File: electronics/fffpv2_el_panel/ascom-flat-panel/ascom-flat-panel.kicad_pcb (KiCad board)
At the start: 2 copper layers, 55 x 46.6 mm, 20 parts, among them J1 Servo, J2 Conn_01x02, Q1 IRLZ34N, Q2 IRLZ34N, U1 XIAO-SAMD21-DIP, U2 TLC272

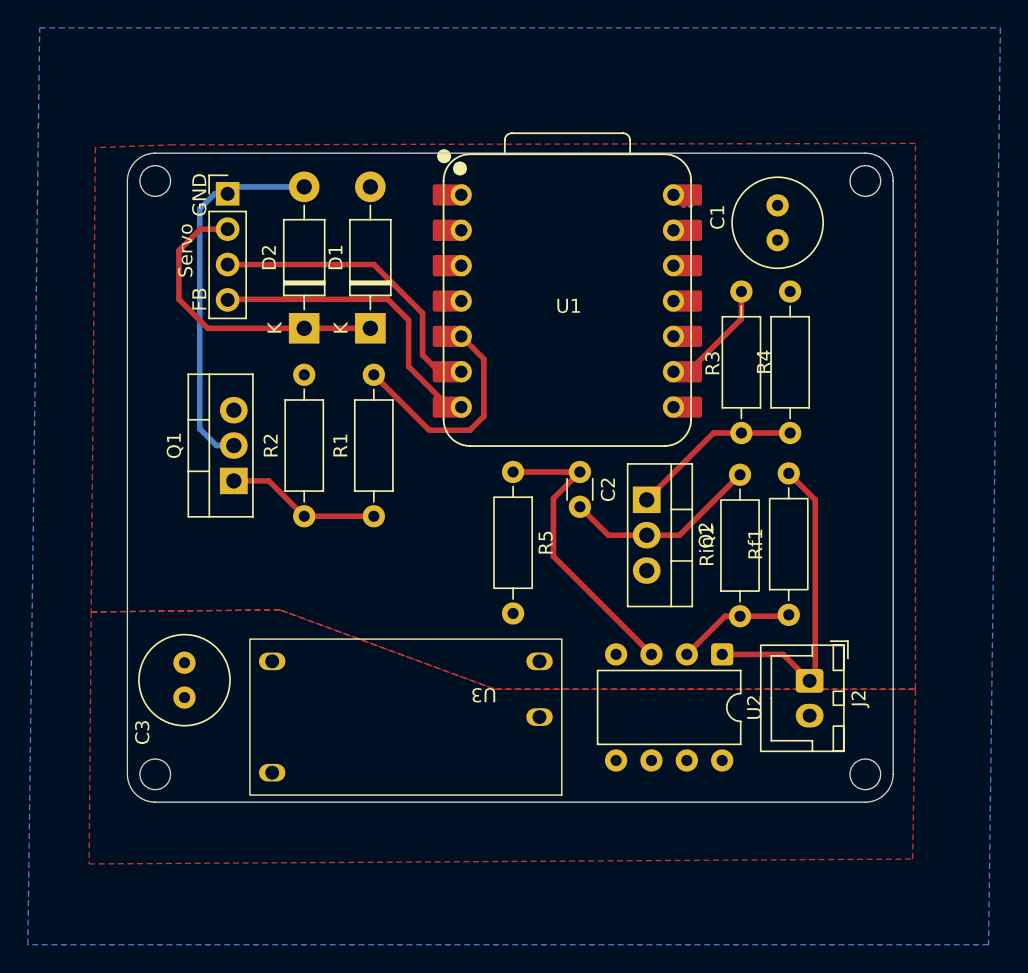
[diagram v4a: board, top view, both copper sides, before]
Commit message: Correction de l'empreinte du convertisseur DC DC + ajustements inhérents sur PCB + corrections cosmétiques sur PCB
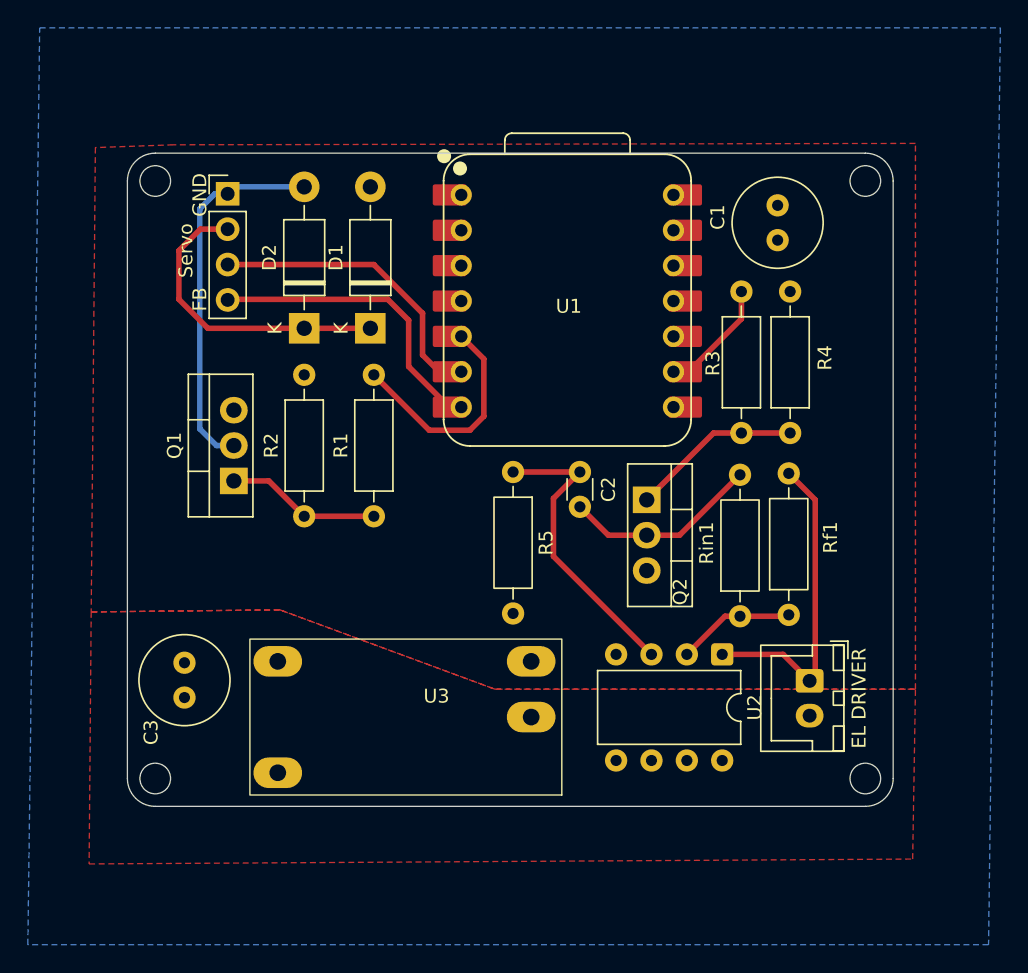
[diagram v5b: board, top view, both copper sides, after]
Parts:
- EL DRIVER: renamed from J2
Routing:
- net +5V: track 2.60 -> 0.48 mm
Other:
- board size 55 x 46.6 mm -> 55 x 46.9 mm

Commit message: Removed most warnings form ERC (schema) and DRC (pcb)
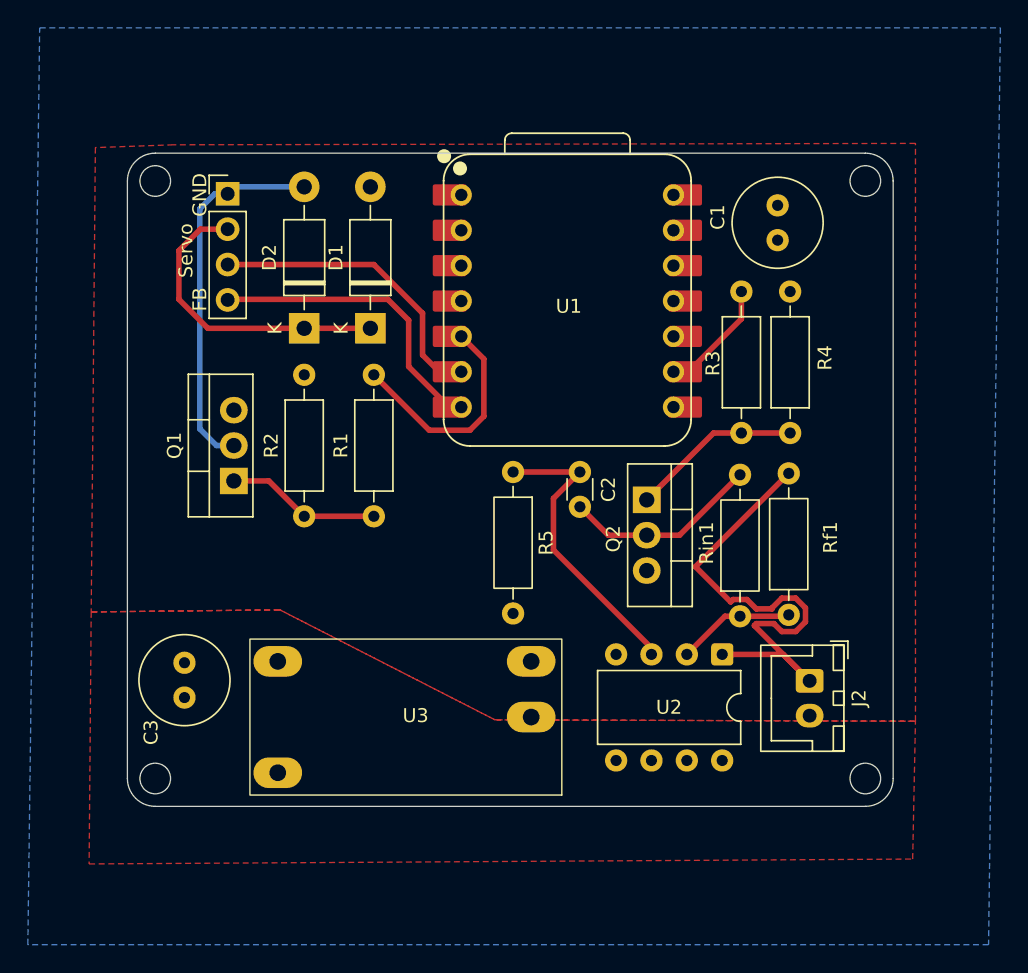
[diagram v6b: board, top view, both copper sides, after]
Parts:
- J2: renamed from EL DRIVER
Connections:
- U2 pad 5: (no net) -> unconnected-(U2B-+-Pad5)
- U2 pad 6: (no net) -> unconnected-(U2B---Pad6)
- U2 pad 7: (no net) -> unconnected-(U2-Pad7)
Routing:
- net EL_DRIVER+: track 22.9 -> 37.4 mm
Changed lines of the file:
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@@
 	(net 22 "EL_DRIVER+")
 	(net 23 "Net-(U2A--)")
+	(net 24 "unconnected-(U1-PA02_A0_D0-Pad1)_1")
+	(net 25 "unconnected-(U1-PB09_A7_D7_RX-Pad8)_1")
+	(net 26 "unconnected-(U1-PA4_A1_D1-Pad2)_1")
+	(net 27 "unconnected-(U1-PA6_A10_D10_MOSI-Pad11)_1")
+	(net 28 "unconnected-(U1-3V3-Pad12)_1")
+	(net 29 "unconnected-(U1-PA5_A9_D9_MISO-Pad10)_1")
+	(net 30 "unconnected-(U1-PA11_A3_D3-Pad4)_1")
+	(net 31 "unconnected-(U1-PA10_A2_D2-Pad3)_1")
+	(net 32 "unconnected-(U2B---Pad6)")
+	(net 33 "unconnected-(U2-Pad7)")
+	(net 34 "unconnected-(U2B-+-Pad5)")
 	(footprint "Connector_JST:JST_XH_B2B-XH-A_1x02_P2.50mm_Vertical"
 		(layer "F.Cu")
@@
 		(descr "JST XH series connector, B2B-XH-A (http://www.jst-mfg.com/product/pdf/eng/eXH.pdf), generated with kicad-footprint-generator")
 		(tags "connector JST XH vertical")
-		(property "Reference" "EL DRIVER"
+		(property "Reference" "J2"
 			(at 1.25 -3.55 90)
 			(layer "F.SilkS")
@@
 			(layers "F.Cu" "F.Mask")
 			(roundrect_rratio 0.1)
-			(net 15 "unconnected-(U1-PA02_A0_D0-Pad1)")
+			(net 24 "unconnected-(U1-PA02_A0_D0-Pad1)_1")
 			(pinfunction "PA02_A0_D0")
-			(pintype "passive")
+			(pintype "passive+no_connect")
 			(thermal_bridge_angle 45)
 		)
@@
 			(net 15 "unconnected-(U1-PA02_A0_D0-Pad1)")
 			(pinfunction "PA02_A0_D0")
-			(pintype "passive")
+			(pintype "passive+no_connect")
 		)
 		(pad "2" smd roundrect
@@
 			(layers "F.Cu" "F.Mask")
 			(roundrect_rratio 0.1)
-			(net 16 "unconnected-(U1-PA4_A1_D1-Pad2)")
+			(net 26 "unconnected-(U1-PA4_A1_D1-Pad2)_1")
 			(pinfunction "PA4_A1_D1")
-			(pintype "passive")
+			(pintype "passive+no_connect")
 			(thermal_bridge_angle 45)
 		)
@@
 			(net 16 "unconnected-(U1-PA4_A1_D1-Pad2)")
 			(pinfunction "PA4_A1_D1")
-			(pintype "passive")
+			(pintype "passive+no_connect")
 		)
 		(pad "3" smd roundrect
@@
 			(net 14 "unconnected-(U1-PA10_A2_D2-Pad3)")
 			(pinfunction "PA10_A2_D2")
-			(pintype "passive")
+			(pintype "passive+no_connect")
 			(thermal_bridge_angle 45)
 		)
@@
 			(layers "*.Cu" "*.Mask")
 			(remove_unused_layers no)
-			(net 14 "unconnected-(U1-PA10_A2_D2-Pad3)")
+			(net 31 "unconnected-(U1-PA10_A2_D2-Pad3)_1")
 			(pinfunction "PA10_A2_D2")
-			(pintype "passive")
+			(pintype "passive+no_connect")
 		)
 		(pad "4" smd roundrect
@@
 			(net 12 "unconnected-(U1-PA11_A3_D3-Pad4)")
 			(pinfunction "PA11_A3_D3")
-			(pintype "passive")
+			(pintype "passive+no_connect")
 			(thermal_bridge_angle 45)
 		)
@@
 			(layers "*.Cu" "*.Mask")
 			(remove_unused_layers no)
-			(net 12 "unconnected-(U1-PA11_A3_D3-Pad4)")
+			(net 30 "unconnected-(U1-PA11_A3_D3-Pad4)_1")
 			(pinfunction "PA11_A3_D3")
-			(pintype "passive")
+			(pintype "passive+no_connect")
 		)
 		(pad "5" smd roundrect
@@
 			(net 17 "unconnected-(U1-PB09_A7_D7_RX-Pad8)")
 			(pinfunction "PB09_A7_D7_RX")
-			(pintype "passive")
+			(pintype "passive+no_connect")
 		)
 		(pad "8" smd roundrect
@@
 			(layers "F.Cu" "F.Mask")
 			(roundrect_rratio 0.1)
-			(net 17 "unconnected-(U1-PB09_A7_D7_RX-Pad8)")
+			(net 25 "unconnected-(U1-PB09_A7_D7_RX-Pad8)_1")
 			(pinfunction "PB09_A7_D7_RX")
-			(pintype "passive")
+			(pintype "passive+no_connect")
 			(thermal_bridge_angle 45)
 		)
@@
 			(net 13 "unconnected-(U1-PA5_A9_D9_MISO-Pad10)")
 			(pinfunction "PA5_A9_D9_MISO")
-			(pintype "passive")
+			(pintype "passive+no_connect")
 		)
 		(pad "10" smd roundrect
@@
 			(layers "F.Cu" "F.Mask")
 			(roundrect_rratio 0.1)
-			(net 13 "unconnected-(U1-PA5_A9_D9_MISO-Pad10)")
+			(net 29 "unconnected-(U1-PA5_A9_D9_MISO-Pad10)_1")
 			(pinfunction "PA5_A9_D9_MISO")
-			(pintype "passive")
+			(pintype "passive+no_connect")
 			(thermal_bridge_angle 45)
 		)
@@
 			(layers "*.Cu" "*.Mask")
 			(remove_unused_layers no)
-			(net 18 "unconnected-(U1-PA6_A10_D10_MOSI-Pad11)")
+			(net 27 "unconnected-(U1-PA6_A10_D10_MOSI-Pad11)_1")
 			(pinfunction "PA6_A10_D10_MOSI")
-			(pintype "passive")
+			(pintype "passive+no_connect")
 		)
 		(pad "11" smd roundrect
@@
 			(net 18 "unconnected-(U1-PA6_A10_D10_MOSI-Pad11)")
 			(pinfunction "PA6_A10_D10_MOSI")
-			(pintype "passive")
+			(pintype "passive+no_connect")
 			(thermal_bridge_angle 45)
 		)
@@
 			(layers "*.Cu" "*.Mask")
 			(remove_unused_layers no)
-			(net 7 "unconnected-(U1-3V3-Pad12)")
+			(net 28 "unconnected-(U1-3V3-Pad12)_1")
 			(pinfunction "3V3")
-			(pintype "passive")
+			(pintype "passive+no_connect")
 		)
 		(pad "12" smd roundrect
@@
 			(net 7 "unconnected-(U1-3V3-Pad12)")
 			(pinfunction "3V3")
-			(pintype "passive")
+			(pintype "passive+no_connect")
 			(thermal_bridge_angle 45)
 		)
@@
 		(tags "THT DIP DIL PDIP 2.54mm 7.62mm 300mil")
 		(property "Reference" "U2"
-			(at 3.81 -2.33 90)
+			(at 3.8 3.82 0)
 			(layer "F.SilkS")
 			(effects
@@
 			(layers "*.Cu" "*.Mask")
 			(remove_unused_layers no)
+			(net 34 "unconnected-(U2B-+-Pad5)")
+			(pinfunction "+")
+			(pintype "input+no_connect")
 		)
 		(pad "6" thru_hole circle
@@
 			(layers "*.Cu" "*.Mask")
 			(remove_unused_layers no)
+			(net 32 "unconnected-(U2B---Pad6)")
+			(pinfunction "-")
+			(pintype "input+no_connect")
 		)
 		(pad "7" thru_hole circle
@@
 			(layers "*.Cu" "*.Mask")
 			(remove_unused_layers no)
+			(net 33 "unconnected-(U2-Pad7)")
+			(pintype "output+no_connect")
 		)
 		(pad "8" thru_hole circle
@@
 		(tags "TO-220-3 Vertical RM 2.54mm")
 		(property "Reference" "Q2"
-			(at 6.6 -2.4 90)
+			(at 2.8 2.4 90)
 			(layer "F.SilkS")
 			(effects
@@
 		(at 116.3 110.6 180)
 		(property "Reference" "U3"
-			(at -2.2 1.6 0)
+			(at -0.7 0.2 0)
 			(unlocked yes)
 			(layer "F.SilkS")
@@
 	)
 	(segment
-		(start 126.9 94.8)
-		(end 126.9 98.96)
+		(start 128.8 92.9)
+		(end 126.9 94.8)
 		(width 0.4)
 		(layer "F.Cu")
@@
 	)
 	(segment
-		(start 126.9 98.96)
-		(end 133.94 106)
+		(start 126.9 98.5)
+		(end 133.94 105.54)
 		(width 0.4)
 		(layer "F.Cu")
@@
 	)
 	(segment
-		(start 128.8 92.9)
-		(end 126.9 94.8)
+		(start 124 92.9)
+		(end 128.8 92.9)
 		(width 0.4)
 		(layer "F.Cu")
@@
 	)
 	(segment
-		(start 124 92.9)
-		(end 128.8 92.9)
+		(start 126.9 94.8)
+		(end 126.9 98.5)
+		(width 0.4)
+		(layer "F.Cu")
+		(net 19)
+	)
+	(segment
+		(start 133.94 105.54)
+		(end 133.94 106)
 		(width 0.4)
 		(layer "F.Cu")
@@
 	(segment
 		(start 145.3 107.9)
-		(end 145.7 107.5)
+		(end 141.329235 103.929235)
+		(width 0.4)
+		(layer "F.Cu")
+		(net 22)
+	)
+	(segment
+		(start 145.001 102.662529)
+		(end 144.297471 101.959)
+		(width 0.4)
+		(layer "F.Cu")
+		(net 22)
+	)
+	(segment
+		(start 145.001 103.657471)
+		(end 145.001 102.662529)
+		(width 0.4)
+		(layer "F.Cu")
+		(net 22)
+	)
+	(segment
+		(start 140.797471 102.059)
+		(end 139.802529 102.059)
+		(width 0.4)
+		(layer "F.Cu")
+		(net 22)
+	)
+	(segment
+		(start 143.302529 101.959)
+		(end 142.599 102.662529)
+		(width 0.4)
+		(layer "F.Cu")
+		(net 22)
+	)
+	(segment
+		(start 144.297471 101.959)
+		(end 143.302529 101.959)
+		(width 0.4)
+		(layer "F.Cu")
+		(net 22)
+	)
+	(segment
+		(start 142.599 102.732)
+		(end 141.470471 102.732)
+		(width 0.4)
+		(layer "F.Cu")
+		(net 22)
+	)
+	(segment
+		(start 144.297471 104.361)
+		(end 145.001 103.657471)
+		(width 0.4)
+		(layer "F.Cu")
+		(net 22)
+	)
+	(segment
+		(start 141.470471 102.732)
+		(end 140.797471 102.059)
+		(width 0.4)
+		(layer "F.Cu")
+		(net 22)
+	)
+	(segment
+		(start 137.1 99.7)
+		(end 143.8 93)
 		(width 0.4)
 		(layer "F.Cu")
@@
 	)
 	(segment
+		(start 142.599 102.662529)
+		(end 142.599 102.732)
+		(width 0.4)
+		(layer "F.Cu")
+		(net 22)
+	)
+	(segment
+		(start 142.729529 103.788)
+		(end 143.302529 104.361)
+		(width 0.4)
+		(layer "F.Cu")
+		(net 22)
+	)
+	(segment
+		(start 141.470471 103.788)
+		(end 142.729529 103.788)
+		(width 0.4)
+		(layer "F.Cu")
+		(net 22)
+	)
+	(segment
 		(start 143.4 106)
 		(end 145.3 107.9)
@@
 	)
 	(segment
-		(start 145.7 94.9)
-		(end 143.8 93)
+		(start 143.302529 104.361)
+		(end 144.297471 104.361)
+		(width 0.4)
+		(layer "F.Cu")
+		(net 22)
+	)
+	(segment
+		(start 139.630764 102.230764)
+		(end 137.1 99.7)
+		(width 0.4)
+		(layer "F.Cu")
+		(net 22)
+	)
+	(segment
+		(start 141.329235 103.929235)
+		(end 141.470471 103.788)
 		(width 0.4)
 		(layer "F.Cu")
@@
 	)
 	(segment
-		(start 145.7 107.5)
-		(end 145.7 94.9)
+		(start 139.802529 102.059)
+		(end 139.630764 102.230764)
 		(width 0.4)
 		(layer "F.Cu")
@@
 		(polygon
 			(pts
-				(xy 93.7 102.95) (xy 93.55 121.05) (xy 152.7 120.7) (xy 152.9 108.5) (xy 122.7 108.5) (xy 107.25 102.8)
+				(xy 93.7 102.95) (xy 93.55 121.05) (xy 152.7 120.7) (xy 152.9 110.8) (xy 122.7 110.7) (xy 107.25 102.8)
 			)
 		)
@@
 		(polygon
 			(pts
-				(xy 94 69.6) (xy 93.7 102.95) (xy 107.25 102.8) (xy 122.7 108.5) (xy 152.9 108.5) (xy 152.9 69.3)
+				(xy 94 69.6) (xy 93.7 102.95) (xy 107.25 102.8) (xy 122.7 110.7) (xy 152.9 110.8) (xy 152.9 69.3)
 				(xy 99.6 69.4)
 			)

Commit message: Feedback from first breadboard prototype
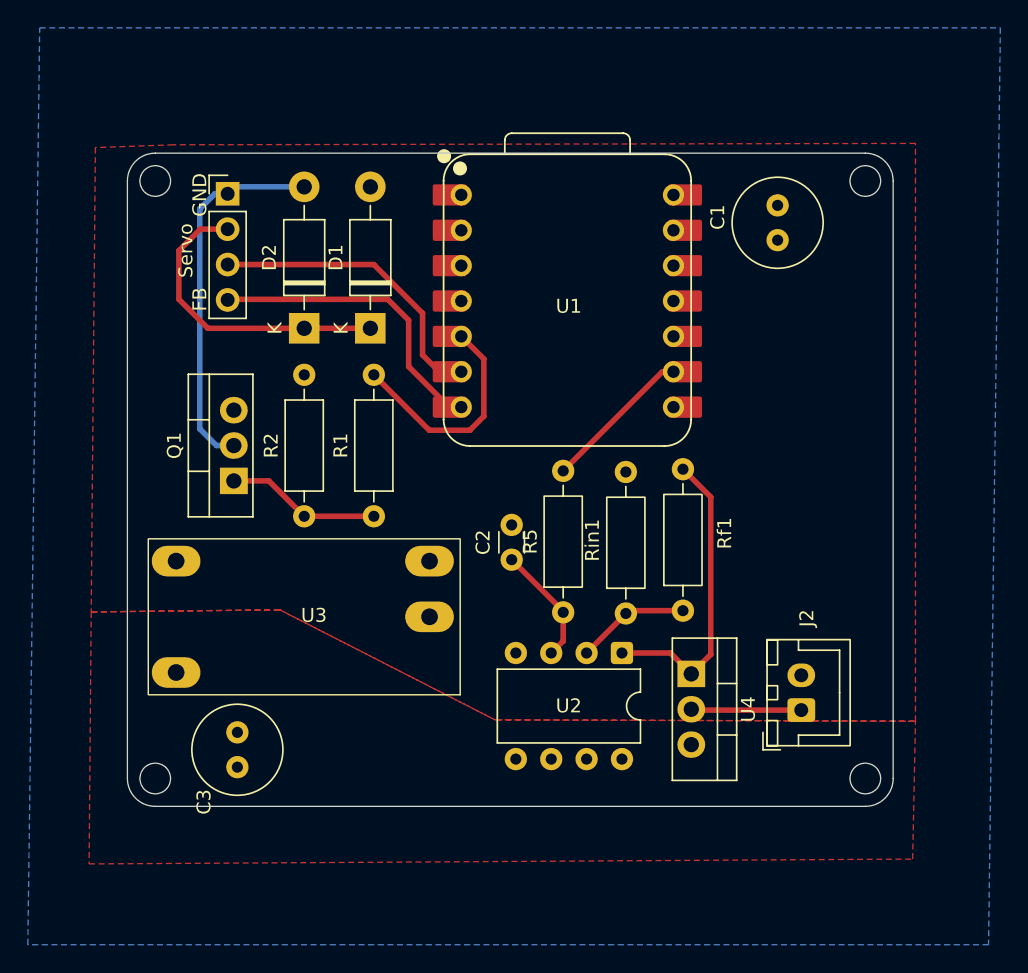
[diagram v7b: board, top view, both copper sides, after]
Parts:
- removed Q2: IRLZ34N, Package_TO_SOT_THT:TO-220-3_Vertical
- removed R3: 330Ω, Resistor_THT:R_Axial_DIN0207_L6.3mm_D2.5mm_P10.16mm_Horizontal
- removed R4: 4.7kΩ, Resistor_THT:R_Axial_DIN0207_L6.3mm_D2.5mm_P10.16mm_Horizontal
- added U4: LM317, Package_TO_SOT_THT:TO-220-3_Vertical, F.Cu at (136.8, 107.4)
- moved R5 10.7 mm to (127.6, 103.0), turned to 90 degrees
- moved U3 10.3 mm to (109.0, 103.4)
- moved Rin1 8.20 mm to (132.1, 103.1)
- moved C2 7.98 mm to (123.9, 99.2), turned to 90 degrees
- moved Rf1 7.61 mm to (136.2, 102.9)
- moved U2 7.20 mm to (131.8, 105.9)
- moved C3 6.28 mm to (104.2, 114.1)
- moved J2 2.18 mm to (144.7, 110.0), turned to 90 degrees
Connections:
- C2 pad 2: EL PANEL CONTROL CIRCUIT -> GND
- R5 pad 2: +5V -> LED_STRIP_POWER_CONTROL
- Rf1 pad 2: EL_DRIVER+ -> Net-(U4-ADJ)
- Rin1 pad 2: EL PANEL CONTROL CIRCUIT -> GND
- U2 pad 1: EL_DRIVER+ -> Net-(U4-ADJ)
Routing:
- net EL_DRIVER+: track 37.4 -> 7.98 mm
- net Net-(U4-ADJ): track 0.00 -> 21.7 mm
- net EL PANEL CONTROL CIRCUIT: track 14.1 -> 0.00 mm
- net Net-(U2A-+): track 21.6 -> 8.89 mm
- net Net-(Q2-G): track 12.3 -> 0.00 mm
- net LED_STRIP_POWER_CONTROL: track 8.41 -> 11.9 mm

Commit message: Updatong shcematics and PCB to use DAC for EL driver PWR ctrl
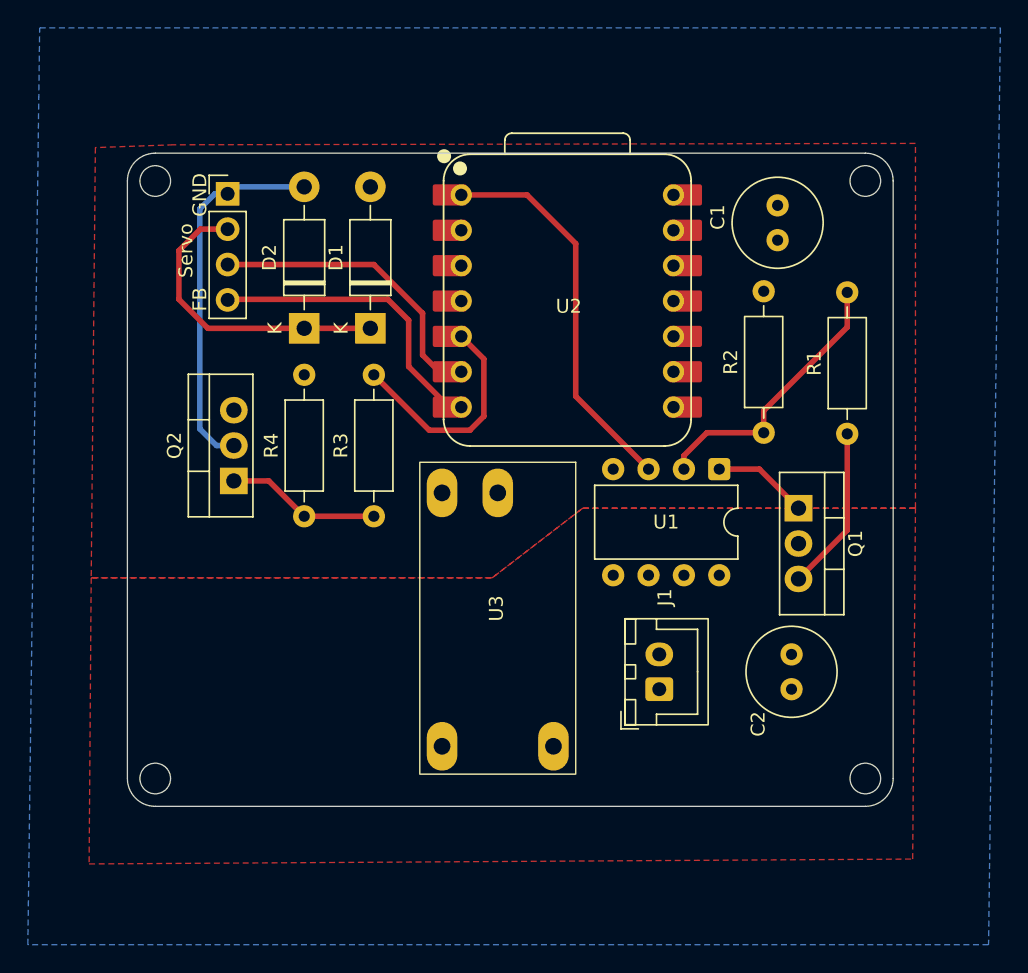
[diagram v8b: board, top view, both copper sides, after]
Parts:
- removed the C2 at (123.9, 99.2)
- removed R5: 1M, Resistor_THT:R_Axial_DIN0207_L6.3mm_D2.5mm_P10.16mm_Horizontal
- removed Rf1: 82k, Resistor_THT:R_Axial_DIN0207_L6.3mm_D2.5mm_P10.16mm_Horizontal
- removed Rin1: 38kΩ, Resistor_THT:R_Axial_DIN0207_L6.3mm_D2.5mm_P10.16mm_Horizontal
- removed U4: LM317, Package_TO_SOT_THT:TO-220-3_Vertical
- added Q1: TIP120, Package_TO_SOT_THT:TO-220-3_Vertical, F.Cu at (144.5, 95.5)
- added R1: 82k, Resistor_THT:R_Axial_DIN0207_L6.3mm_D2.5mm_P10.16mm_Horizontal, F.Cu at (148.0, 90.2)
- added R2: 33k, Resistor_THT:R_Axial_DIN0207_L6.3mm_D2.5mm_P10.16mm_Horizontal, F.Cu at (142.0, 90.1)
- moved C2 40.2 mm to (144.0, 108.5)
- moved U1 14.9 mm to (138.8, 92.7)
- moved U3 14.0 mm to (123.0, 103.4), turned to -90 degrees
- moved J1 10.3 mm to (134.5, 108.5)
- renumbered C3 to C2, J2 to J1, J1 to J2, Q1 to Q2, R1 to R3, R2 to R4, U2 to U1, U1 to U2
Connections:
- U1 pad 3: Net-(U2A-+) -> DAC_PANEL_POWER_CONTROL
- U2 pad 1: unconnected-(U1-PA02_A0_D0-Pad1) -> DAC_PANEL_POWER_CONTROL
- U2 pad 9: LED_STRIP_POWER_CONTROL -> unconnected-(U2-PA7_A8_D8_SCK-Pad9)
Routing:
- net DAC_PANEL_POWER_CONTROL: track 0.00 -> 28.0 mm
- net Net-(Q1-B): track 21.7 -> 6.85 mm
- net LED_STRIP_POWER_CONTROL: track 11.9 -> 0.00 mm
- net Net-(Q1-E): track 0.00 -> 11.9 mm
- net Net-(U1A--): track 8.19 -> 19.9 mm
- net Net-(U2A-+): track 8.89 -> 0.00 mm
- net EL_DRIVER+: track 7.98 -> 0.00 mm
- net (no net): track 0.00 -> 1.08 mm
